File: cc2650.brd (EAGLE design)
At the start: 50.8 x 22.9 mm, 26 parts, among them IC1 TPS73133DBVR, IC4 CC2650MODAMOHR, SW1 SPST_TACT-KMR2, SW3 SPST_TACT-KMR2

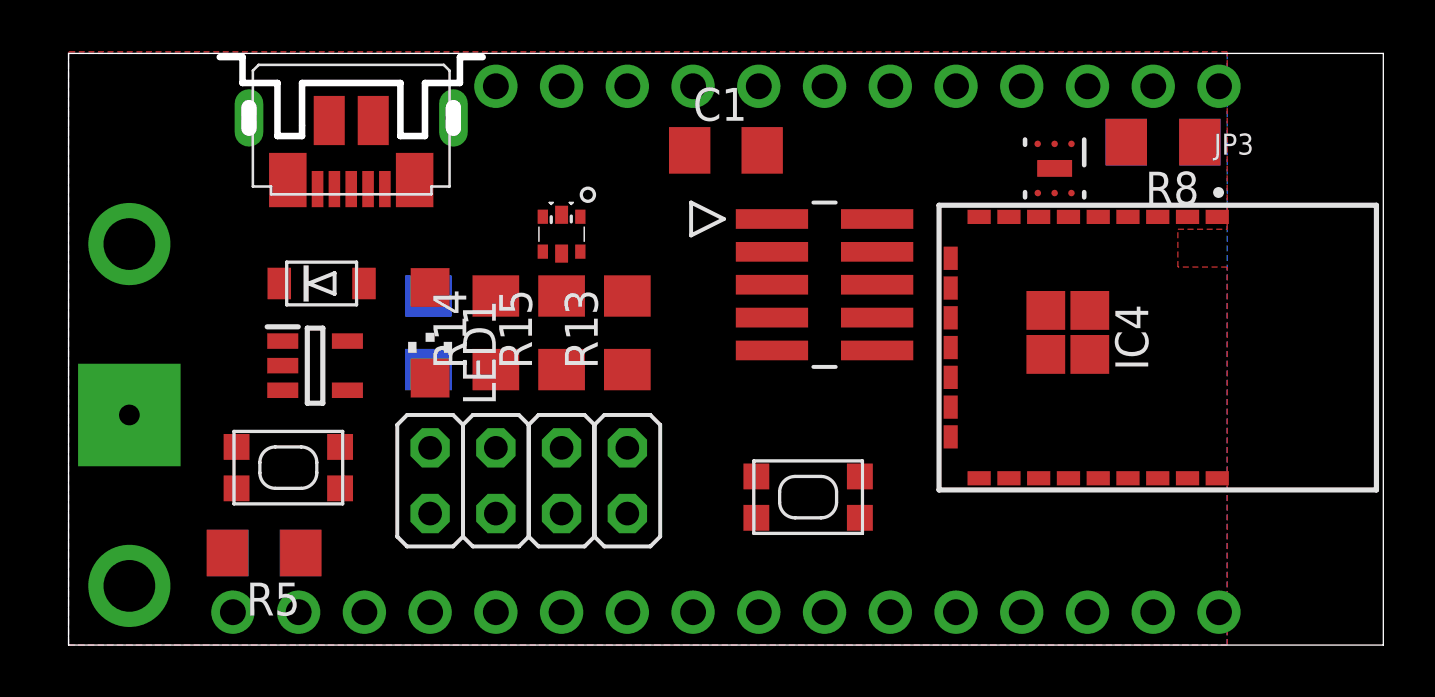
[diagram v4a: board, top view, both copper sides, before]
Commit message: added 100k res between EN and VBUS and added EN to pin headers. Changed coin cell holder to external connector.
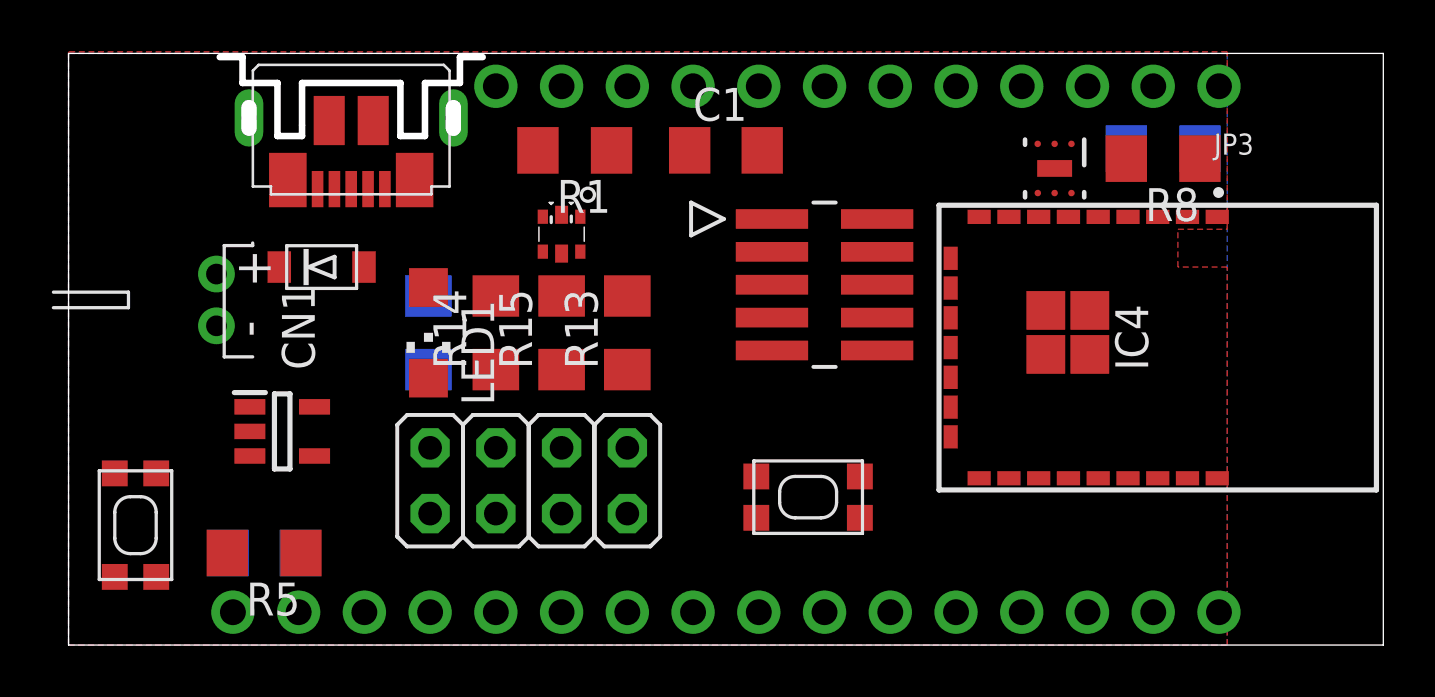
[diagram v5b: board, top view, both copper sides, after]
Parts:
- removed U$1: (no value), adafruit:CR1220-THM
- added CN1: (no value), adafruit:JST-PH-2-THM-RA
- added R1: 100k, adafruit:R1206
- moved SW1 6.31 mm to (2.59, 4.63), turned to 90 degrees
- moved IC1 2.84 mm to (8.26, 8.26)
- moved R8 0.64 mm to (42.3, 18.8)
- moved D2 0.63 mm to (9.78, 14.6)
- moved R7 0.25 mm to (42.3, 19.2)
- moved LED1 0.06 mm to (13.9, 12.1)
- turned C3 to 180 degrees
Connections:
- removed net N$9: JP3.11
- new net EN: IC1.3, JP3.11, R1.2
- net GND: now also CN1.2; no longer U$1.-
- net VBAT: now also CN1.1; no longer U$1.+1, U$1.+2
- net VBUS: now also R1.1; no longer IC1.3

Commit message: switched usb and battery connection to match real feather layout. moved some other components to compensate.
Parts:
- moved R1 16.7 mm to (8.76, 6.41)
- moved USB101 14.3 mm to (1.02, 11.4), turned to 90 degrees
- moved D2 9.38 mm to (18.0, 19.1), turned to 180 degrees
- moved CN1 5.99 mm to (10.8, 16.5), turned to 0 degrees
- moved IC1 2.29 mm to (9.53, 10.2), turned to 90 degrees
- moved SW1 1.27 mm to (2.59, 3.36)

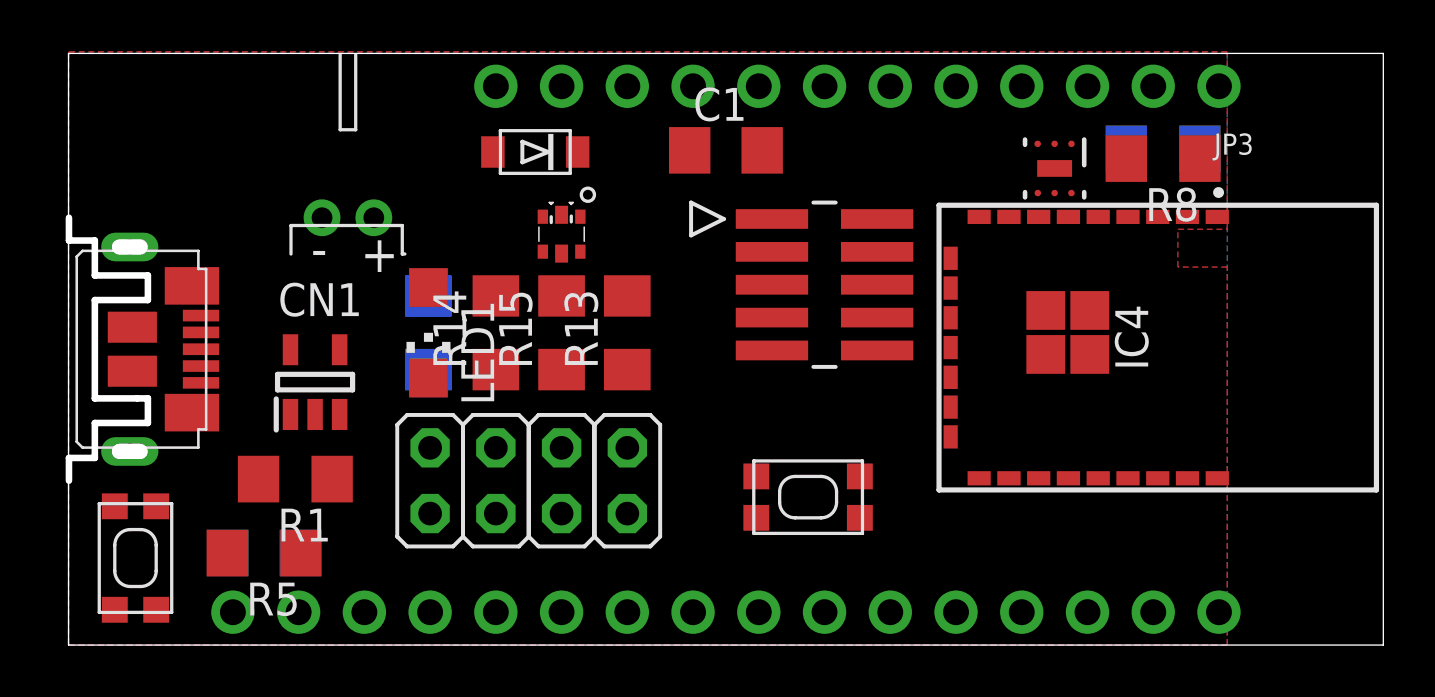
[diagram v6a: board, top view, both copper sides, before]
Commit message: modified adafruit FeatehrWing pin part to remove bottom left hole. Swapped modified FeatherWing for the 1x12 & 1x16 pin headers.
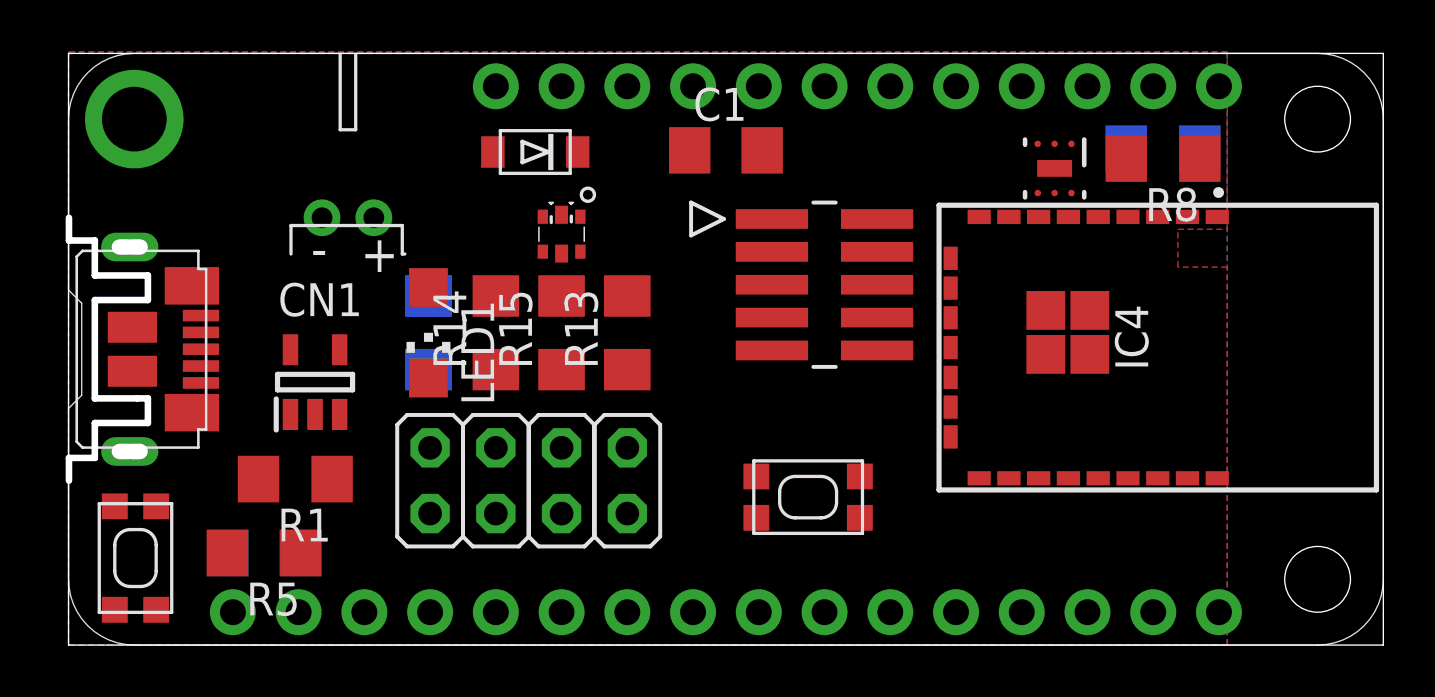
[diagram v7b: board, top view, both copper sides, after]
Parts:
- removed JP2: (no value), microbuilder:1X16_ROUND
- removed JP3: (no value), microbuilder:1X12_ROUND
- added MS1: FEATHERWING_NODIM, wing_modified:FEATHERWING_DIM
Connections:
- net DIO0_TX: now also MS1.15; no longer JP2.15
- net DIO10_CLK: now also MS1.11; no longer JP2.11
- net DIO11_MOSI: now also MS1.12; no longer JP2.12
- net DIO12_MISO: now also MS1.13; no longer JP2.13
- net DIO13: now also MS1.22; no longer JP3.6
- net DIO14: now also MS1.9; no longer JP2.9
- net DIO1_RX: now also MS1.14; no longer JP2.14
- net DIO2: now also MS1.17; no longer JP3.1
- net DIO3: now also MS1.18; no longer JP3.2
- net DIO4: now also MS1.19; no longer JP3.3
- net DIO5_TDO: now also MS1.5; no longer JP2.5
- net DIO6_TDI: now also MS1.6; no longer JP2.6
- net DIO7: now also MS1.20; no longer JP3.4
- net DIO8: now also MS1.21; no longer JP3.5
- net DIO9_CS: now also MS1.10; no longer JP2.10
- net EN: now also MS1.27; no longer JP3.11
- net GND: now also MS1.16, MS1.23, MS1.24, MS1.4; no longer JP2.16, JP2.4, JP3.7, JP3.8
- net JTAG_TCK: now also MS1.8; no longer JP2.8
- net JTAG_TMS: now also MS1.7; no longer JP2.7
- net NRESET: now also MS1.1; no longer JP2.1
- net VBAT: now also MS1.28; no longer JP3.12
- net VBUS: now also MS1.26; no longer JP3.10
- net VCC: now also MS1.2, MS1.25, MS1.3; no longer JP2.2, JP2.3, JP3.9
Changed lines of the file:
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@@
 <attribute name="OC_NEWARK" value="58M7854" x="2.5865" y="3.3625" size="1.778" layer="27" rot="R90" display="off"/>
-</element>
-<element name="JP3" library="microbuilder" package="1X12_ROUND" value="" x="30.48" y="21.59" rot="R180">
-<attribute name="MF" value="" x="30.48" y="21.59" size="1.778" layer="27" rot="R180" display="off"/>
-<attribute name="MPN" value="" x="30.48" y="21.59" size="1.778" layer="27" rot="R180" display="off"/>
-<attribute name="OC_NEWARK" value="unknown" x="30.48" y="21.59" size="1.778" layer="27" rot="R180" display="off"/>
-</element>
-<element name="JP2" library="microbuilder" package="1X16_ROUND" value="" x="25.4" y="1.27" rot="MR180">
-<attribute name="MF" value="" x="25.4" y="1.27" size="1.778" layer="28" rot="MR180" display="off"/>
-<attribute name="MPN" value="3002" x="25.4" y="1.27" size="1.778" layer="28" rot="MR180" display="off"/>
-<attribute name="OC_NEWARK" value="48AC7804" x="25.4" y="1.27" size="1.778" layer="28" rot="MR180" display="off"/>
 </element>
 <element name="USB101" library="MSP_Connectors" package="MOLEX_105164-0001" value="" x="1.016" y="11.43" rot="R90">
@@
 </element>
 <element name="CN1" library="adafruit" package="JST-PH-2-THM-RA" value="" x="10.795" y="16.51"/>
+<element name="MS1" library="wing_modified" package="FEATHERWING_DIM" value="FEATHERWING_NODIM" x="0" y="0"/>
 </elements>
 <signals>
@@
 <vertex x="44.7675" y="22.9235"/>
 </polygon>
-<contactref element="JP2" pad="16"/>
-<contactref element="JP2" pad="4"/>
 <contactref element="C1" pad="2"/>
-<contactref element="JP3" pad="8"/>
-<contactref element="JP3" pad="7"/>
 <contactref element="LED1" pad="C"/>
 <contactref element="IC1" pad="2"/>
 <contactref element="CN1" pad="2"/>
+<contactref element="MS1" pad="24"/>
+<contactref element="MS1" pad="23"/>
+<contactref element="MS1" pad="4"/>
+<contactref element="MS1" pad="16"/>
 <wire x1="42.084" y1="16.5435" x2="44.384" y2="16.5435" width="0" layer="19" extent="1-1"/>
 <wire x1="38.1" y1="18.415" x2="42.084" y2="16.5435" width="0" layer="19" extent="1-1"/>
@@
 <contactref element="C3" pad="1"/>
 <contactref element="R5" pad="2"/>
-<contactref element="JP2" pad="1"/>
+<contactref element="MS1" pad="1"/>
 <wire x1="31.242" y1="11.382" x2="34.084" y2="11.4935" width="0" layer="19" extent="1-1"/>
 <wire x1="6.1565" y1="3.556" x2="31.242" y2="11.382" width="0" layer="19" extent="1-16"/>
@@
 <contactref element="IC4" pad="9"/>
 <contactref element="JTAG_CONNECTOR" pad="2"/>
-<contactref element="JP2" pad="7"/>
+<contactref element="MS1" pad="7"/>
 <wire x1="31.242" y1="16.462" x2="35.184" y2="16.5435" width="0" layer="19" extent="1-1"/>
 <wire x1="21.59" y1="1.27" x2="31.242" y2="16.462" width="0" layer="19" extent="1-1"/>
@@
 <contactref element="JTAG_CONNECTOR" pad="4"/>
 <contactref element="IC4" pad="10"/>
-<contactref element="JP2" pad="8"/>
+<contactref element="MS1" pad="8"/>
 <wire x1="31.242" y1="15.192" x2="34.084" y2="14.9435" width="0" layer="19" extent="1-1"/>
 <wire x1="24.13" y1="1.27" x2="31.242" y2="15.192" width="0" layer="19" extent="1-1"/>
@@
 <contactref element="IC4" pad="11"/>
 <contactref element="JTAG_CONNECTOR" pad="6"/>
-<contactref element="JP2" pad="5"/>
+<contactref element="MS1" pad="5"/>
 <wire x1="31.242" y1="13.922" x2="34.084" y2="13.7935" width="0" layer="19" extent="1-1"/>
 <wire x1="16.51" y1="1.27" x2="31.242" y2="13.922" width="0" layer="19" extent="1-1"/>
@@
 <contactref element="IC4" pad="12"/>
 <contactref element="JTAG_CONNECTOR" pad="8"/>
-<contactref element="JP2" pad="6"/>
+<contactref element="MS1" pad="6"/>
 <wire x1="31.242" y1="12.652" x2="34.084" y2="12.6435" width="0" layer="19" extent="1-1"/>
 <wire x1="19.05" y1="1.27" x2="31.242" y2="12.652" width="0" layer="19" extent="1-1"/>
@@
 <signal name="DIO7">
 <contactref element="IC4" pad="14"/>
-<contactref element="JP3" pad="4"/>
+<contactref element="MS1" pad="20"/>
 <wire x1="34.084" y1="10.3435" x2="36.83" y2="21.59" width="0" layer="19" extent="1-1"/>
 </signal>
 <signal name="DIO0_TX">
 <contactref element="IC4" pad="4"/>
-<contactref element="JP2" pad="15"/>
+<contactref element="MS1" pad="15"/>
 <wire x1="41.91" y1="1.27" x2="40.934" y2="16.5435" width="0" layer="19" extent="1-1"/>
 </signal>
 <signal name="DIO1_RX">
 <contactref element="IC4" pad="5"/>
-<contactref element="JP2" pad="14"/>
+<contactref element="MS1" pad="14"/>
 <wire x1="39.37" y1="1.27" x2="39.784" y2="16.5435" width="0" layer="19" extent="1-1"/>
 </signal>
 <signal name="DIO2">
 <contactref element="IC4" pad="6"/>
-<contactref element="JP3" pad="1"/>
 <contactref element="OPT3001" pad="6"/>
 <contactref element="R8" pad="1"/>
+<contactref element="MS1" pad="17"/>
 <wire x1="43.713" y1="18.796" x2="44.45" y2="21.59" width="0" layer="19" extent="1-1"/>
 <wire x1="38.75" y1="17.465" x2="43.713" y2="18.796" width="0" layer="19" extent="1-1"/>
@@
 <signal name="DIO3">
 <contactref element="IC4" pad="7"/>
-<contactref element="JP3" pad="2"/>
 <contactref element="OPT3001" pad="4"/>
 <contactref element="R7" pad="1"/>
-<wire x1="43.713" y1="19.177" x2="41.91" y2="21.59" width="0" layer="19" extent="16-16"/>
+<contactref element="MS1" pad="18"/>
+<wire x1="41.91" y1="21.59" x2="43.713" y2="19.177" width="0" layer="19" extent="16-16"/>
 <wire x1="37.45" y1="17.465" x2="41.91" y2="21.59" width="0" layer="19" extent="1-1"/>
 <wire x1="37.484" y1="16.5435" x2="37.45" y2="17.465" width="0" layer="19" extent="1-1"/>
@@
 <signal name="DIO4">
 <contactref element="IC4" pad="8"/>
-<contactref element="JP3" pad="3"/>
+<contactref element="MS1" pad="19"/>
 <wire x1="36.334" y1="16.5435" x2="39.37" y2="21.59" width="0" layer="19" extent="1-1"/>
 </signal>
@@
 <signal name="DIO14">
 <contactref element="IC4" pad="21"/>
-<contactref element="JP2" pad="9"/>
 <contactref element="SW3" pad="2"/>
 <contactref element="SW3" pad="4"/>
+<contactref element="MS1" pad="9"/>
 <wire x1="30.575" y1="4.915" x2="39.784" y2="6.4435" width="0" layer="19" extent="1-1"/>
 <wire x1="26.575" y1="4.915" x2="30.575" y2="4.915" width="0" layer="19" extent="1-1"/>
@@
 <signal name="DIO13">
 <contactref element="IC4" pad="20"/>
-<contactref element="JP3" pad="6"/>
+<contactref element="MS1" pad="22"/>
 <wire x1="38.634" y1="6.4435" x2="31.75" y2="21.59" width="0" layer="19" extent="1-1"/>
 </signal>
 <signal name="DIO12_MISO">
 <contactref element="IC4" pad="19"/>
-<contactref element="JP2" pad="13"/>
+<contactref element="MS1" pad="13"/>
 <wire x1="36.83" y1="1.27" x2="37.484" y2="6.4435" width="0" layer="19" extent="1-1"/>
 </signal>
 <signal name="DIO11_MOSI">
 <contactref element="IC4" pad="18"/>
-<contactref element="JP2" pad="12"/>
+<contactref element="MS1" pad="12"/>
 <wire x1="34.29" y1="1.27" x2="36.334" y2="6.4435" width="0" layer="19" extent="1-1"/>
 </signal>
 <signal name="DIO9_CS">
 <contactref element="IC4" pad="16"/>
-<contactref element="JP2" pad="10"/>
+<contactref element="MS1" pad="10"/>
 <wire x1="29.21" y1="1.27" x2="34.084" y2="8.0435" width="0" layer="19" extent="1-1"/>
 </signal>
 <signal name="DIO10_CLK">
 <contactref element="IC4" pad="17"/>
-<contactref element="JP2" pad="11"/>
+<contactref element="MS1" pad="11"/>
 <wire x1="31.75" y1="1.27" x2="35.184" y2="6.4435" width="0" layer="19" extent="1-1"/>
 </signal>
 <signal name="DIO8">
 <contactref element="IC4" pad="15"/>
-<contactref element="JP3" pad="5"/>
+<contactref element="MS1" pad="21"/>
 <wire x1="34.084" y1="9.1935" x2="34.29" y2="21.59" width="0" layer="19" extent="1-1"/>
 </signal>
@@
 <contactref element="R8" pad="2"/>
 <contactref element="R5" pad="1"/>
-<contactref element="JP2" pad="2"/>
 <contactref element="C1" pad="1"/>
-<contactref element="JP2" pad="3"/>
-<contactref element="JP3" pad="9"/>
 <contactref element="JP1" pad="1"/>
+<contactref element="MS1" pad="25"/>
+<contactref element="MS1" pad="2"/>
+<contactref element="MS1" pad="3"/>
 <wire x1="40.869" y1="18.796" x2="40.869" y2="19.177" width="0" layer="19" extent="1-16"/>
 <wire x1="38.75" y1="19.365" x2="40.869" y2="19.177" width="0" layer="19" extent="1-16"/>
@@
 <signal name="VBAT">
 <contactref element="D2" pad="A"/>
-<contactref element="JP3" pad="12"/>
 <contactref element="CN1" pad="1"/>
+<contactref element="MS1" pad="28"/>
 <wire x1="16.3965" y1="19.05" x2="16.51" y2="21.59" width="0" layer="19" extent="1-1"/>
 <wire x1="11.795" y1="16.51" x2="16.3965" y2="19.05" width="0" layer="19" extent="1-1"/>
@@
 <contactref element="IC1" pad="1"/>
 <contactref element="D2" pad="C"/>
-<contactref element="JP3" pad="10"/>
 <contactref element="R1" pad="1"/>
+<contactref element="MS1" pad="26"/>
 <wire x1="19.6715" y1="19.05" x2="21.59" y2="21.59" width="0" layer="19" extent="1-1"/>
 <wire x1="8.575" y1="8.91" x2="19.6715" y2="19.05" width="0" layer="19" extent="1-1"/>
@@
 </signal>
 <signal name="EN">
-<contactref element="JP3" pad="11"/>
 <contactref element="IC1" pad="3"/>
 <contactref element="R1" pad="2"/>
+<contactref element="MS1" pad="27"/>
 <wire x1="10.475" y1="8.91" x2="19.05" y2="21.59" width="0" layer="19" extent="1-1"/>
 <wire x1="7.341" y1="6.4135" x2="10.475" y2="8.91" width="0" layer="19" extent="1-1"/>
